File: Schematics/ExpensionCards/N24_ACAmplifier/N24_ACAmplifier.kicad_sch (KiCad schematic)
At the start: 45 parts

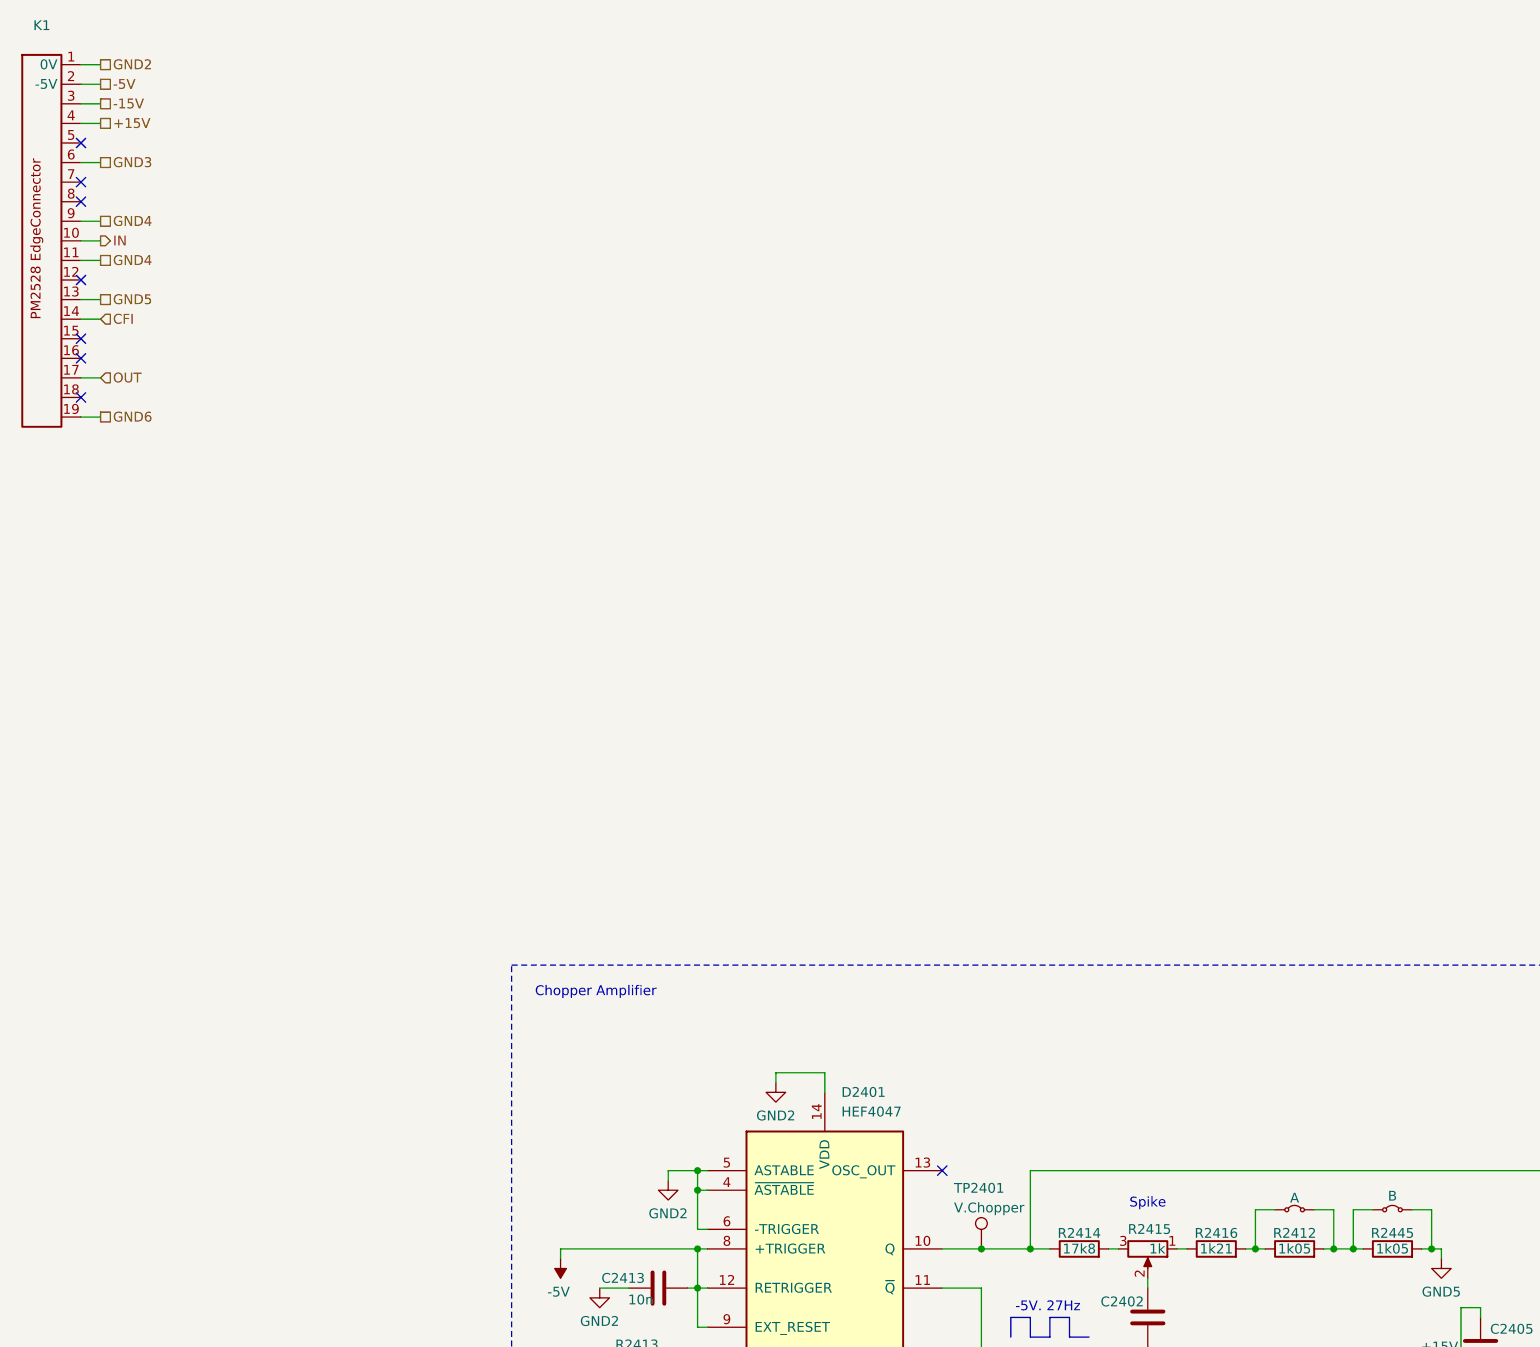
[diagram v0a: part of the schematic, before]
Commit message: Reworked N20/N21
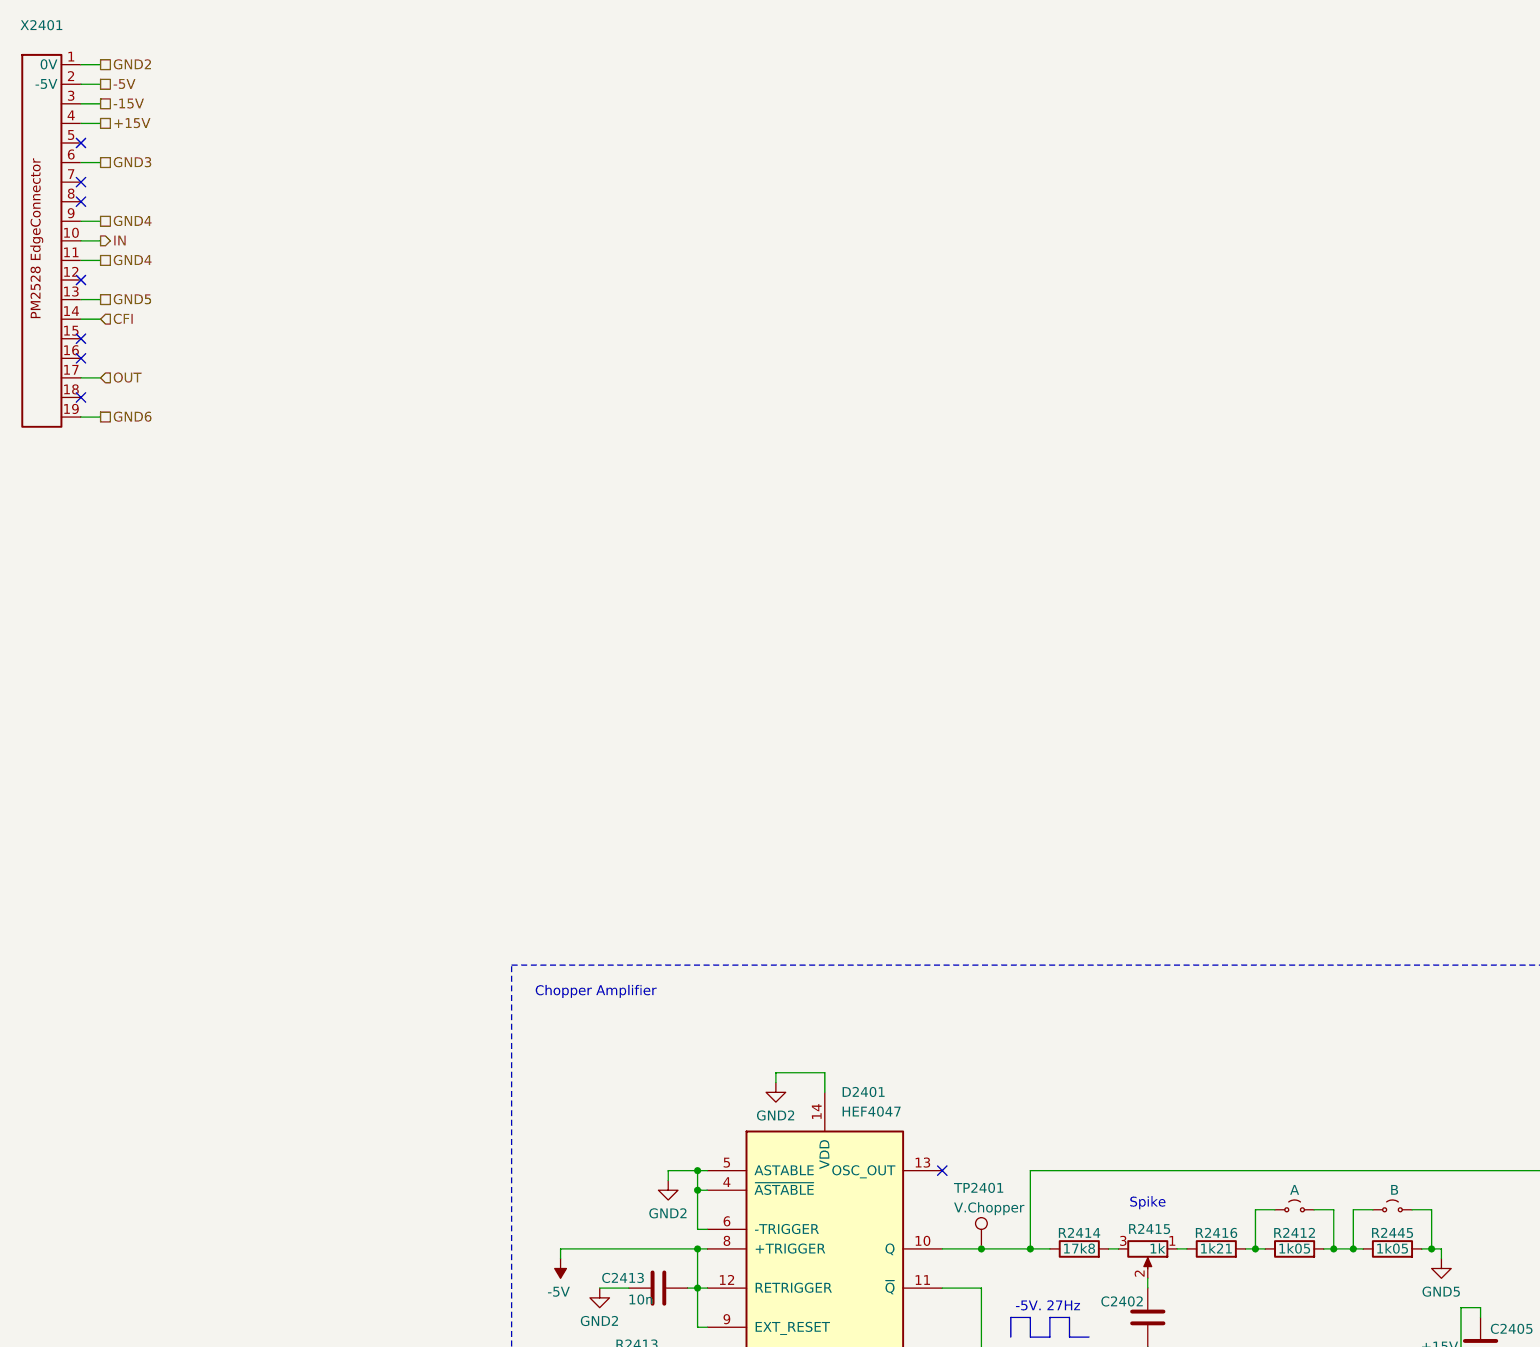
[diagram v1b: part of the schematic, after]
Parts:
- JP2401: renamed from JP1; footprint TestPoint:TestPoint_Bridge_Pitch2.54mm_Drill1.0mm -> TestPoint:TestPoint_Bridge_Pitch5.08mm_Drill0.7mm; symbol Jumper:Jumper_2_Small_Bridged -> Jumper:Jumper_2_Small_Open
- JP2402: renamed from JP2; footprint TestPoint:TestPoint_Bridge_Pitch2.54mm_Drill1.0mm -> TestPoint:TestPoint_Bridge_Pitch5.08mm_Drill0.7mm; symbol Jumper:Jumper_2_Small_Bridged -> Jumper:Jumper_2_Small_Open
- R2406, R2415: footprint (none) -> PM2528:Trimmer vertical
- TP2401, TP2402, TP2403, TP2405, TP2406: footprint TestPoint:TestPoint_Loop_D2.50mm_Drill1.0mm -> Connector_Pin:Pin_D0.9mm_L10.0mm_W2.4mm_FlatFork
- renumbered K1 to X2401
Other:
- company: (none) -> D. Kupers
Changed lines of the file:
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@@
 	(title_block
 		(title "Philips PM2528 - N24 (AC Amplifier)")
-		(date "2025-07-06")
+		(date "2025-08-06")
 		(rev "0.1")
+		(company "D. Kupers")
 	)
 	(rectangle
@@
 		(dnp no)
 		(fields_autoplaced yes)
-		(property "Reference" "K1"
+		(property "Reference" "X2401"
 			(at 20.32 29.21 0)
 			(effects
@@
 					(size 1.27 1.27)
 				)
+				(hide yes)
 			)
 		)
@@
 			(project ""
 				(path "/10314dd0-d63b-49c9-902d-69ff1737d02f"
-					(reference "K1")
+					(reference "X2401")
 					(unit 1)
 				)
@@
 			)
 		)
-		(property "Footprint" "TestPoint:TestPoint_Loop_D2.50mm_Drill1.0mm"
+		(property "Footprint" "Connector_Pin:Pin_D0.9mm_L10.0mm_W2.4mm_FlatFork"
 			(at 276.86 215.9 0)
 			(effects
@@
 			)
 		)
-		(property "Footprint" "TestPoint:TestPoint_Loop_D2.50mm_Drill1.0mm"
+		(property "Footprint" "Connector_Pin:Pin_D0.9mm_L10.0mm_W2.4mm_FlatFork"
 			(at 229.87 215.9 0)
 			(effects
@@
 			)
 		)
-		(property "Footprint" ""
+		(property "Footprint" "PM2528:Trimmer vertical"
 			(at 137.16 228.6 0)
 			(effects
@@
 	)
 	(symbol
-		(lib_id "Jumper:Jumper_2_Small_Bridged")
+		(lib_id "Jumper:Jumper_2_Small_Open")
 		(at 195.58 182.88 0)
 		(unit 1)
@@
 		(on_board yes)
 		(dnp no)
-		(property "Reference" "JP2"
+		(property "Reference" "JP2402"
 			(at 195.58 176.53 0)
 			(effects
@@
 		)
 		(property "Value" "B"
-			(at 195.58 181.102 0)
+			(at 195.834 180.34 0)
 			(effects
 				(font
@@
 			)
 		)
-		(property "Footprint" "TestPoint:TestPoint_Bridge_Pitch2.54mm_Drill1.0mm"
+		(property "Footprint" "TestPoint:TestPoint_Bridge_Pitch5.08mm_Drill0.7mm"
 			(at 195.58 182.88 0)
 			(effects
@@
 			)
 		)
-		(property "Description" "Jumper, 2-pole, small symbol, bridged"
+		(property "Description" "Jumper, 2-pole, small symbol, open"
 			(at 195.58 182.88 0)
 			(effects
@@
 			(project "N24_ACAmplifier"
 				(path "/10314dd0-d63b-49c9-902d-69ff1737d02f"
-					(reference "JP2")
+					(reference "JP2402")
 					(unit 1)
 				)
@@
 			)
 		)
-		(property "Footprint" ""
+		(property "Footprint" "PM2528:Trimmer vertical"
 			(at 163.83 187.96 0)
 			(effects
@@
 			)
 		)
-		(property "Footprint" "TestPoint:TestPoint_Loop_D2.50mm_Drill1.0mm"
+		(property "Footprint" "Connector_Pin:Pin_D0.9mm_L10.0mm_W2.4mm_FlatFork"
 			(at 147.32 187.96 0)
 			(effects
@@
 	)
 	(symbol
-		(lib_id "Jumper:Jumper_2_Small_Bridged")
+		(lib_id "Jumper:Jumper_2_Small_Open")
 		(at 182.88 182.88 0)
 		(unit 1)
@@
 		(on_board yes)
 		(dnp no)
-		(property "Reference" "JP1"
+		(property "Reference" "JP2401"
 			(at 182.88 176.53 0)
 			(effects
@@
 		)
 		(property "Value" "A"
-			(at 182.88 181.356 0)
+			(at 182.88 180.34 0)
 			(effects
 				(font
@@
 			)
 		)
-		(property "Footprint" "TestPoint:TestPoint_Bridge_Pitch2.54mm_Drill1.0mm"
+		(property "Footprint" "TestPoint:TestPoint_Bridge_Pitch5.08mm_Drill0.7mm"
 			(at 182.88 182.88 0)
 			(effects
@@
 			)
 		)
-		(property "Description" "Jumper, 2-pole, small symbol, bridged"
+		(property "Description" "Jumper, 2-pole, small symbol, open"
 			(at 182.88 182.88 0)
 			(effects
@@
 			(project "N24_ACAmplifier"
 				(path "/10314dd0-d63b-49c9-902d-69ff1737d02f"
-					(reference "JP1")
+					(reference "JP2401")
 					(unit 1)
 				)
@@
 			)
 		)
-		(property "Footprint" "TestPoint:TestPoint_Loop_D2.50mm_Drill1.0mm"
+		(property "Footprint" "Connector_Pin:Pin_D0.9mm_L10.0mm_W2.4mm_FlatFork"
 			(at 252.73 215.9 0)
 			(effects
@@
 			)
 		)
-		(property "Footprint" "TestPoint:TestPoint_Loop_D2.50mm_Drill1.0mm"
+		(property "Footprint" "Connector_Pin:Pin_D0.9mm_L10.0mm_W2.4mm_FlatFork"
 			(at 359.41 237.49 0)
 			(effects

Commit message: Small modifications, more disassembly
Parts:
- added A2402: LM393N, symbol Comparator:LM393
- added C2411: 330n, symbol Device:C
- added C2412: 150p, symbol Device:C
- added C2425: 39p, symbol Device:C
- added R2417: 10m, symbol Device:R
- added R2422: 150, PM2528:Trimmer vertical, symbol Device:R_Potentiometer
- added R2423: 464k, symbol Device:R
- added R2446: 1k21, symbol Device:R
- added R2447, R2448: 15k4, symbol Device:R
- added R2449: 46k4, symbol Device:R
- added R2450, R2453: 30k1, symbol Device:R
- added R2451, R2452: 1k05, symbol Device:R
- added V2404: BFQ14, symbol PM2528:FET_Dual
- added V2419, V2420: BAV45, Diode_THT:D_DO-35_SOD27_P7.62mm_Horizontal, symbol Diode:1N4148
- added V2421, V2422: BAW62, Diode_THT:D_DO-35_SOD27_P7.62mm_Horizontal, symbol Diode:1N4148
- added V2423, V2424: BZX79-B8V2, symbol Device:D_Zener
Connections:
- net +15V: now also A2402.8 (V+), R2447.2, R2453.1
- net -15V: now also A2402.4 (V-), C2425.1, R2423.1, R2448.1, R2450.1
- net CFI: now also A2402.1, A2402.7, C2425.2, R2449.2
- net GND2: now also R2449.1, R2451.1, R2452.1
- net GND3: now also R2446.1
- net IN: now also C2411.2, V2419.2 (A), V2420.1 (K)
- net at R2424.2: now also V2404.6 (G)
- new net: A2402.6 (-), R2450.2, R2451.2
- new net: A2402.2 (-), R2448.2, V2422.2 (A), V2424.2 (A)
- new net: R2446.2, V2419.1 (K), V2420.2 (A), V2421.2 (A), V2422.1 (K)
- new net: A2402.3 (+), R2452.2, R2453.2
- new net: R2422.1, V2404.4 (S)
- new net: R2422.2, R2423.2
- new net: R2422.3, V2404.1 (S)
- new net: C2411.1, R2417.2, V2404.3 (G)
- new net: C2412.1, V2404.5 (D)
- new net: C2412.2, V2404.2 (D)
- new net: V2423.2 (A), V2424.1 (K)
- new net: A2402.5 (+), R2447.1, V2421.1 (K), V2423.1 (K)
- new net GND: R2417.1
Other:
- note added: "-5V/27Hz"
- note added: "Crest Factor Indicator"
- note added: "Ioff"
- note removed: "-5V. 27Hz"
- moved on the sheet: A2401, C2401, C2402, C2403, C2404, C2405, C2406, C2407, C2408, C2409, C2410, C2413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

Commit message: Updated N24 schema/PCB
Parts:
- added C2414: 1n8, Capacitor_THT:C_Disc_D4.3mm_W1.9mm_P5.00mm, symbol Device:C
- added C2415: 15p, Capacitor_THT:C_Disc_D4.3mm_W1.9mm_P5.00mm, symbol Device:C
- added C2416: 12p, Capacitor_THT:C_Disc_D4.3mm_W1.9mm_P5.00mm, symbol Device:C
- added C2417: 10n, Capacitor_THT:C_Disc_D4.3mm_W1.9mm_P5.00mm, symbol Device:C
- added C2418: 560p, Capacitor_THT:C_Disc_D4.3mm_W1.9mm_P5.00mm, symbol Device:C
- added C2419, C2420: 6n8, Capacitor_THT:C_Disc_D4.3mm_W1.9mm_P5.00mm, symbol Device:C
- added JP1: Jumper_2_Small_Bridged, TestPoint:TestPoint_Bridge_Pitch5.08mm_Drill0.7mm, symbol Jumper:Jumper_2_Small_Bridged
- added R2418, R2419: 46k4, Resistor_THT:R_Axial_DIN0207_L6.3mm_D2.5mm_P10.16mm_Horizontal, symbol Device:R
- added R2420, R2421: 8k25, Resistor_THT:R_Axial_DIN0207_L6.3mm_D2.5mm_P10.16mm_Horizontal, symbol Device:R
- added R2425: 2k74, Resistor_THT:R_Axial_DIN0207_L6.3mm_D2.5mm_P10.16mm_Horizontal, symbol Device:R
- added R2426: 1k78, Resistor_THT:R_Axial_DIN0207_L6.3mm_D2.5mm_P10.16mm_Horizontal, symbol Device:R
- added R2427: 140, Resistor_THT:R_Axial_DIN0207_L6.3mm_D2.5mm_P10.16mm_Horizontal, symbol Device:R
- added R2428: 10M, Resistor_THT:R_Axial_DIN0207_L6.3mm_D2.5mm_P10.16mm_Horizontal, symbol Device:R
- added R2429: 301k, Resistor_THT:R_Axial_DIN0207_L6.3mm_D2.5mm_P10.16mm_Horizontal, symbol Device:R
- added R2430: 60k4, Resistor_THT:R_Axial_DIN0207_L6.3mm_D2.5mm_P10.16mm_Horizontal, symbol Device:R
- added R2431, R2437: 2k15, Resistor_THT:R_Axial_DIN0207_L6.3mm_D2.5mm_P10.16mm_Horizontal, symbol Device:R
- added R2432: 205, Resistor_THT:R_Axial_DIN0207_L6.3mm_D2.5mm_P10.16mm_Horizontal, symbol Device:R
- added R2433: 2k61, Resistor_THT:R_Axial_DIN0207_L6.3mm_D2.5mm_P10.16mm_Horizontal, symbol Device:R
- added R2434: 2k37, Resistor_THT:R_Axial_DIN0207_L6.3mm_D2.5mm_P10.16mm_Horizontal, symbol Device:R
- added R2435, R2436: 7R05, Resistor_THT:R_Axial_DIN0207_L6.3mm_D2.5mm_P10.16mm_Horizontal, symbol Device:R
- added R2438: 4k64, Resistor_THT:R_Axial_DIN0207_L6.3mm_D2.5mm_P10.16mm_Horizontal, symbol Device:R
- added R2439: 215, Resistor_THT:R_Axial_DIN0207_L6.3mm_D2.5mm_P10.16mm_Horizontal, symbol Device:R
- added R2440, R2441, R2443, R2444: 71R5, Resistor_THT:R_Axial_DIN0207_L6.3mm_D2.5mm_P10.16mm_Horizontal, symbol Device:R
- added R2442: 21R15, Resistor_THT:R_Axial_DIN0207_L6.3mm_D2.5mm_P10.16mm_Horizontal, symbol Device:R
- added TP2404: something, Connector_Pin:Pin_D0.9mm_L10.0mm_W2.4mm_FlatFork, symbol Connector:TestPoint
- added TP2407: OUT, Connector_Pin:Pin_D0.9mm_L10.0mm_W2.4mm_FlatFork, symbol Connector:TestPoint
- added V2405, V2406, V2413: BC547B, Package_TO_SOT_THT:TO-92_Inline, symbol Transistor_BJT:BC547
- added V2407, V2408: BC557B, Package_TO_SOT_THT:TO-92_Inline, symbol Transistor_BJT:BC557
- added V2409, V2410: BFW11, Package_TO_SOT_THT:TO-72-4, symbol Transistor_FET:BF245C
- added V2411, V2412, V2415: BF199, Package_TO_SOT_THT:TO-92_Inline, symbol Transistor_BJT:BC547
- added V2416: BF324, Package_TO_SOT_THT:TO-92_Inline, symbol Transistor_BJT:BC557
- added V2417: BZX79-C3V0, Diode_THT:D_DO-35_SOD27_P10.16mm_Horizontal, symbol Device:D_Zener
- added V2418: BZV46-C2V0, Diode_THT:D_DO-35_SOD27_P10.16mm_Horizontal, symbol Device:D_Zener
- A2402: footprint (none) -> Package_DIP:DIP-8_W7.62mm
- C2401, C2403, C2406: footprint (none) -> Capacitor_THT:C_Rect_L13.0mm_W4.0mm_P10.00mm_FKS3_FKP3_MKS4
- C2402, C2404, C2405, C2412, C2413, C2421, C2422, C2423, C2424, C2425: footprint (none) -> Capacitor_THT:C_Disc_D4.3mm_W1.9mm_P5.00mm
- C2407: footprint (none) -> Capacitor_THT:CP_Radial_Tantal_D4.5mm_P5.00mm; symbol Device:C -> Device:C_Polarized
- C2408: footprint (none) -> Capacitor_THT:C_Axial_L5.1mm_D3.1mm_P15.00mm_Horizontal
- C2409, C2410: footprint (none) -> Capacitor_THT:CP_Radial_Tantal_D4.5mm_P5.00mm
- C2411: footprint (none) -> Capacitor_THT:C_Rect_L18.0mm_W5.0mm_P15.00mm_FKS3_FKP3
- R2401, R2402, R2403, R2404, R2405, R2407, R2408, R2409, R2410, R2411, R2412, R2413, R2414, R2416, R2424, R2445, R2446, R2447, R2448, R2449, R2450, R2451, R2452, R2453: footprint (none) -> Resistor_THT:R_Axial_DIN0207_L6.3mm_D2.5mm_P10.16mm_Horizontal
- R2417: value 10m -> 10M; footprint (none) -> Resistor_THT:R_Axial_DIN0207_L6.3mm_D2.5mm_P10.16mm_Horizontal
- R2423: value 464k -> 46k4; footprint (none) -> Resistor_THT:R_Axial_DIN0207_L6.3mm_D2.5mm_P10.16mm_Horizontal
- TP2401: value V.Chopper -> Fchop
- V2404: footprint (none) -> Package_TO_SOT_THT:TO-75-6
- V2419, V2420: footprint Diode_THT:D_DO-35_SOD27_P7.62mm_Horizontal -> Package_TO_SOT_THT:TO-72-4
- V2421, V2422: footprint Diode_THT:D_DO-35_SOD27_P7.62mm_Horizontal -> Diode_THT:D_DO-35_SOD27_P10.16mm_Horizontal
- V2423, V2424: footprint (none) -> Diode_THT:D_DO-35_SOD27_P10.16mm_Horizontal
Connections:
- net GND is gone; now on net GND2: R2417.1
- net +15V: now also C2419.2, R2418.2, R2419.2, R2425.2, R2433.2, R2434.2, V2405.1 (C), V2406.1 (C), V2415.1 (C)
- net -15V: now also C2420.1, R2426.1, R2430.1, R2431.1, R2437.1, R2439.1, V2407.1 (C), V2416.1 (C), V2417.2 (A)
- net GND2: now also C2414.1, R2420.1, R2421.1, R2429.1, V2409.2 (S), V2410.2 (S)
- net GND4: now also V2402.2 (S); no longer V2402.3 (D)
- net GND5: now also R2438.1
- net GND6: now also C2419.1, C2420.2
- net OUT: now also V2423.2 (A), V2424.1 (K), C2418.1, R2443.1, R2444.2, TP2407.1
- net at R2410.2, R2411.1, TP2402.1: now also V2402.3 (D); no longer V2402.2 (S)
- net at C2411.1, R2417.2, V2404.3 (G): now also C2415.1
- net at C2412.1, V2404.5 (D): now also R2419.1, V2406.2 (B)
- net at C2412.2, V2404.2 (D): now also R2418.1, V2405.2 (B)
- new net: C2415.2, R2428.2, V2409.1 (G)
- new net: R2431.2, V2409.3 (D), V2411.2 (B)
- new net: C2416.2, C2417.1, R2441.1, R2442.1, V2411.1 (C), V2418.1 (K)
- new net: C2418.2, R2442.2
- new net: R2444.1, V2416.3 (E)
- new net: C2417.2, R2433.1, R2440.1, V2418.2 (A)
- new net: C2416.1, R2432.1
- new net: R2435.1, V2411.3 (E)
- new net: R2432.2, R2434.1, V2412.1 (C)
- new net: R2437.2, V2410.3 (D), V2412.2 (B)
- new net: R2436.2, V2412.3 (E)
- new net: R2425.1, V2407.3 (E), V2408.3 (E)
- new net: JP1.2 (B), TP2404.1, V2410.1 (G)
- new net: R2428.1, R2429.2, R2430.2
- new net: R2440.2, V2415.2 (B)
- new net: R2443.2, V2415.3 (E)
- new net: R2438.2, V2413.2 (B), V2417.1 (K)
- new net: R2420.2, V2405.3 (E), V2407.2 (B)
- new net: R2435.2, R2436.1, V2413.1 (C)
- new net: R2439.2, V2413.3 (E)
- new net: R2441.2, V2416.2 (B)
- new net: JP1.1 (A), R2426.2, R2427.2, V2408.1 (C)
- new net: R2421.2, V2406.3 (E), V2408.2 (B)
- new net: C2414.2, R2427.1
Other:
- moved on the sheet: A2402A, A2402B, A2402C, C2409, C2410, C2421, C2422, C2423, C2424, C2425, R2446, R2447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
